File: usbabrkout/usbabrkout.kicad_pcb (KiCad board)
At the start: 4 copper layers, 27.7 x 20.3 mm, 12 parts, among them P101 CONN_01X01, P102 CONN_01X01, P103 CONN_01X01, P104 CONN_01X01, P105 USB_A

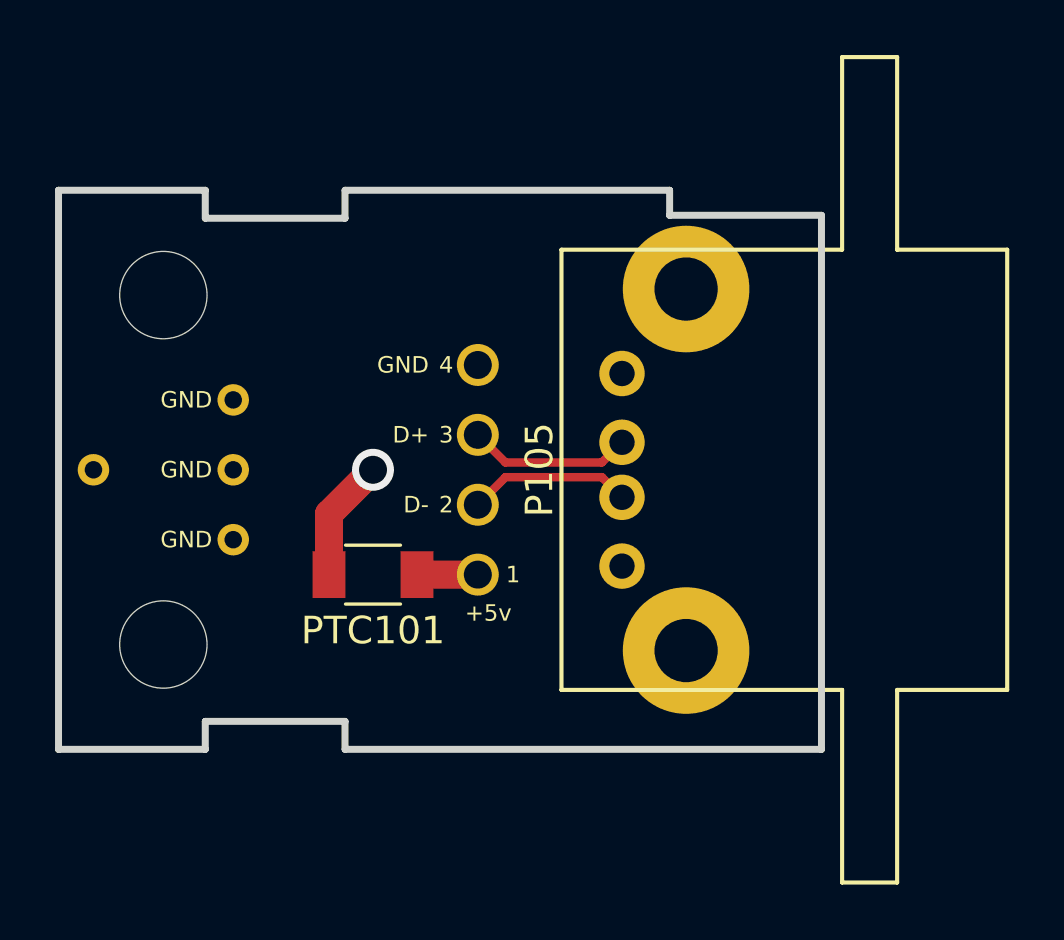
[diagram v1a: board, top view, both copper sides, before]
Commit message: Update usbabrkout design to KiCad 8.
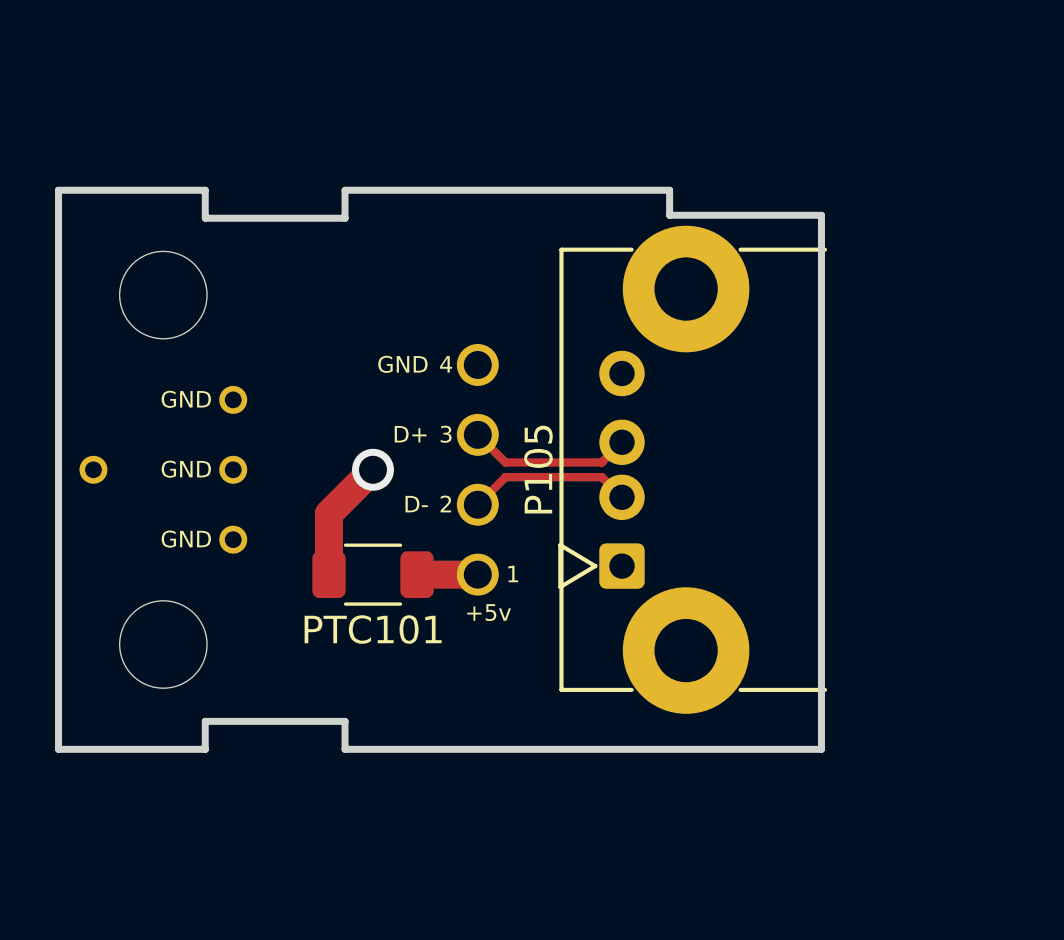
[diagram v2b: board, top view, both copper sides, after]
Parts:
- P101, P102, P103, P104: footprint local:wire_60x40mil -> Local:wire_60x40mil
- P105: footprint local:usb-a-pm -> Local:usb-a-pm
- PTC101: footprint local:R_1206_HandSoldering -> Local:R_1206_HandSoldering
- REF** (x2): footprint local:MountingHole_125mil -> Local:MountingHole_125mil
- REF** (x4): footprint local:Stitching_Via_40x24mil -> Local:Stitching_Via_40x24mil
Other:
- net class Default removed
- net class Diff Pair removed
- net class minimum removed
- board text added: "dsun7c4osh@gmail.com"
- board text removed: "dcsun88osh@gmail.com"

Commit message: Bump version string of usbabrkout to v1.1.0.
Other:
- board text added: "v1.1.0"
- board text removed: "v1.0.0"
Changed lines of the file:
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@@
 	(title_block
 		(title "USB-A panel mount breakout")
-		(date "2018-04-23")
-		(rev "v1.0.0")
+		(date "2025-01-27")
+		(rev "v1.1.0")
 	)
 	(layers
@@
 			)
 		)
+		(property "Voltage" ""
+			(at 0 0 90)
+			(unlocked yes)
+			(layer "F.Fab")
+			(hide yes)
+			(effects
+				(font
+					(size 1 1)
+					(thickness 0.15)
+				)
+			)
+		)
+		(property "Tolerance" ""
+			(at 0 0 90)
+			(unlocked yes)
+			(layer "F.Fab")
+			(hide yes)
+			(effects
+				(font
+					(size 1 1)
+					(thickness 0.15)
+				)
+			)
+		)
+		(property "Dielectric" ""
+			(at 0 0 90)
+			(unlocked yes)
+			(layer "F.Fab")
+			(hide yes)
+			(effects
+				(font
+					(size 1 1)
+					(thickness 0.15)
+				)
+			)
+		)
+		(property "Power" ""
+			(at 0 0 90)
+			(unlocked yes)
+			(layer "F.Fab")
+			(hide yes)
+			(effects
+				(font
+					(size 1 1)
+					(thickness 0.15)
+				)
+			)
+		)
+		(property "Current" ""
+			(at 0 0 90)
+			(unlocked yes)
+			(layer "F.Fab")
+			(hide yes)
+			(effects
+				(font
+					(size 1 1)
+					(thickness 0.15)
+				)
+			)
+		)
+		(property "Frequency" ""
+			(at 0 0 90)
+			(unlocked yes)
+			(layer "F.Fab")
+			(hide yes)
+			(effects
+				(font
+					(size 1 1)
+					(thickness 0.15)
+				)
+			)
+		)
 		(property ki_fp_filters "USB*")
 		(sheetname "Root")
@@
 		(layer "Edge.Cuts")
 	)
-	(gr_text "v1.0.0"
+	(gr_text "v1.1.0"
 		(at 142.24 95.25 0)
 		(layer "B.SilkS")
